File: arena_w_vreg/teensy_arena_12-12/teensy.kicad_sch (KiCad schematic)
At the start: 3 parts, among them J2 Conn_01x04, J3 Conn_01x04, U13 Teensy4.1

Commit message: Added new pcb routing for 12-12 with vreg.
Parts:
- J2, J3: footprint Connector_JST:JST_SH_SM04B-SRSS-TB_1x04-1MP_P1.00mm_Horizontal -> arena_custom:JST_SH_SM04B-SRSS-TB_1x04-1MP_P1.00mm_Horizontal
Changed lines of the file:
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@@
       (effects (font (size 1.27 1.27)) (justify left))
     )
-    (property "Footprint" "Connector_JST:JST_SH_SM04B-SRSS-TB_1x04-1MP_P1.00mm_Horizontal" (at 136.652 149.606 0)
+    (property "Footprint" "arena_custom:JST_SH_SM04B-SRSS-TB_1x04-1MP_P1.00mm_Horizontal" (at 136.652 149.606 0)
       (effects (font (size 1.27 1.27)) hide)
     )
@@
       (effects (font (size 1.27 1.27)) (justify left))
     )
-    (property "Footprint" "Connector_JST:JST_SH_SM04B-SRSS-TB_1x04-1MP_P1.00mm_Horizontal" (at 81.534 150.368 0)
-      (effects (font (size 1.27 1.27)) hide)
-    )
+    (property "Footprint" "arena_custom:JST_SH_SM04B-SRSS-TB_1x04-1MP_P1.00mm_Horizontal" (at 81.534 150.368 0)
+      (effects (font (size 1.27 1.27)) hide)
+    )

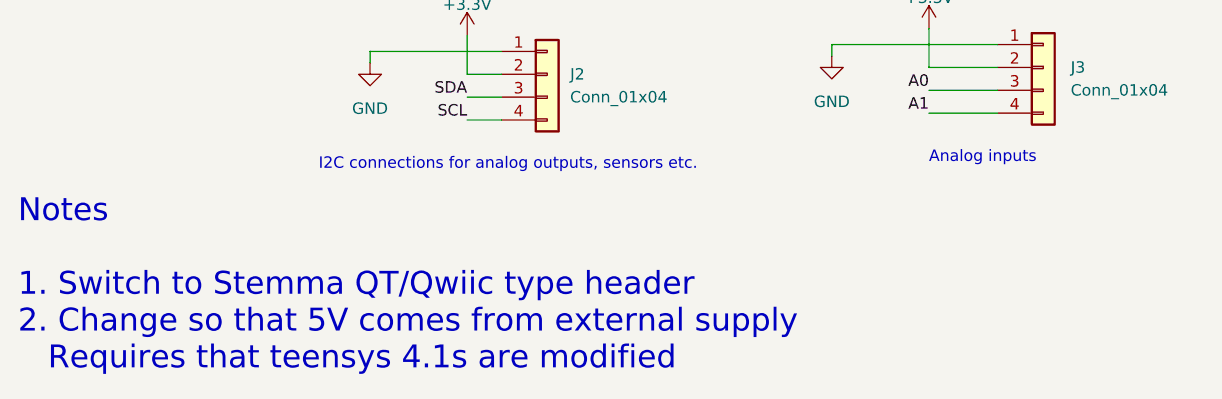
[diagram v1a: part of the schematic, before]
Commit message: Removed old notes from schematic pdf.
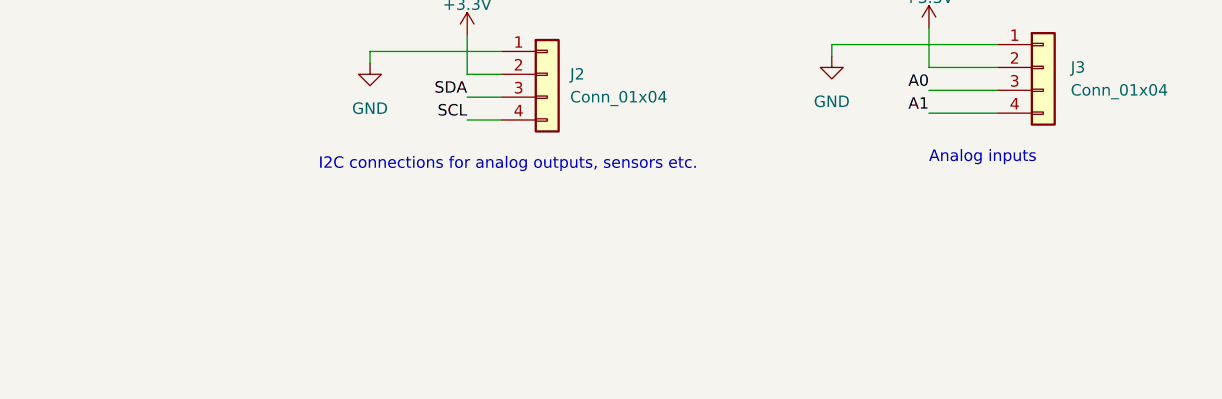
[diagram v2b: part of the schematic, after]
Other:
- note removed: "Notes 1. Switch to Stemma QT/Qwiic type header 2. Change so that 5V comes from external supply Requires that teensys 4.1s are modified"
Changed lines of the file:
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@@
     (stroke (width 0) (type default))
-  )
-  (text "Notes\n\n1. Switch to Stemma QT/Qwiic type header  \n2. Change so that 5V comes from external supply \n   Requires that teensys 4.1s are modified\n\n"
-    (at 22.733 187.579 0)
-    (effects (font (size 2.54 2.54)) (justify left bottom))
   )
   (text "Analog inputs" (at 123.952 160.401 0)
